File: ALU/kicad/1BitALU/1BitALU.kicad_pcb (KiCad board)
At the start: 2 copper layers, 165.1 x 120.7 mm, 55 parts, among them P1 CONN_6, P2 CONN_2, P3 Power, U1 xor3a, U10 and3a, U11 or2a, U12 and3b, U13 inv3b, U14 and3c, U15 or3a, U16 xor1b, U17 xor1a, U18 xor2b, U19 and4a, U2 and2a, U20 xor2a, U21 and4b, U22 and4c, U23 or3b, U24 and5a, U25 and5b, U26 inv5c, U27 and5c, U28 or3c, U29 and6a, U3 xor3b, U30 inv6b, U31 and6b, U32 inv6c, U33 and6c, U34 or3d, U4 and2b, U5 or1b, U6 and1a, U7 and1b, U8 or1a, U9 or2b

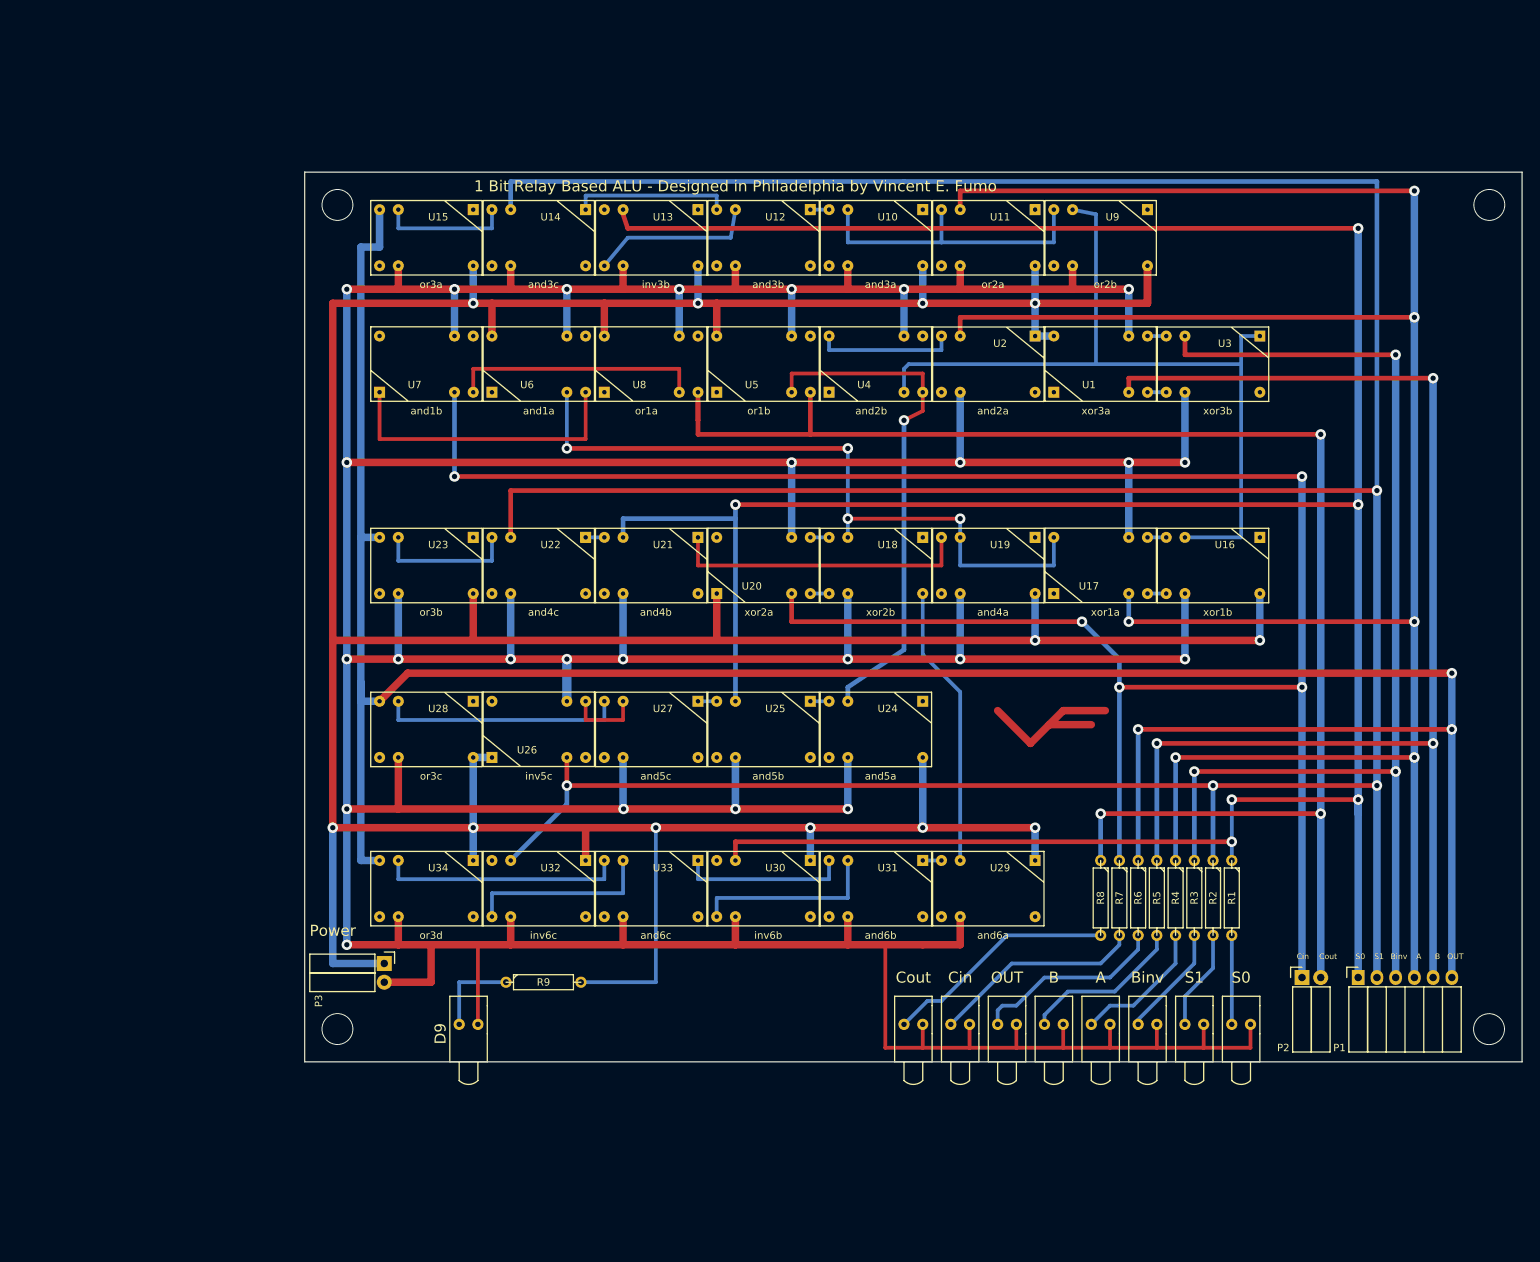
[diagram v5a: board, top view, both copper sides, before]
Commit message: puts bus connectors on side
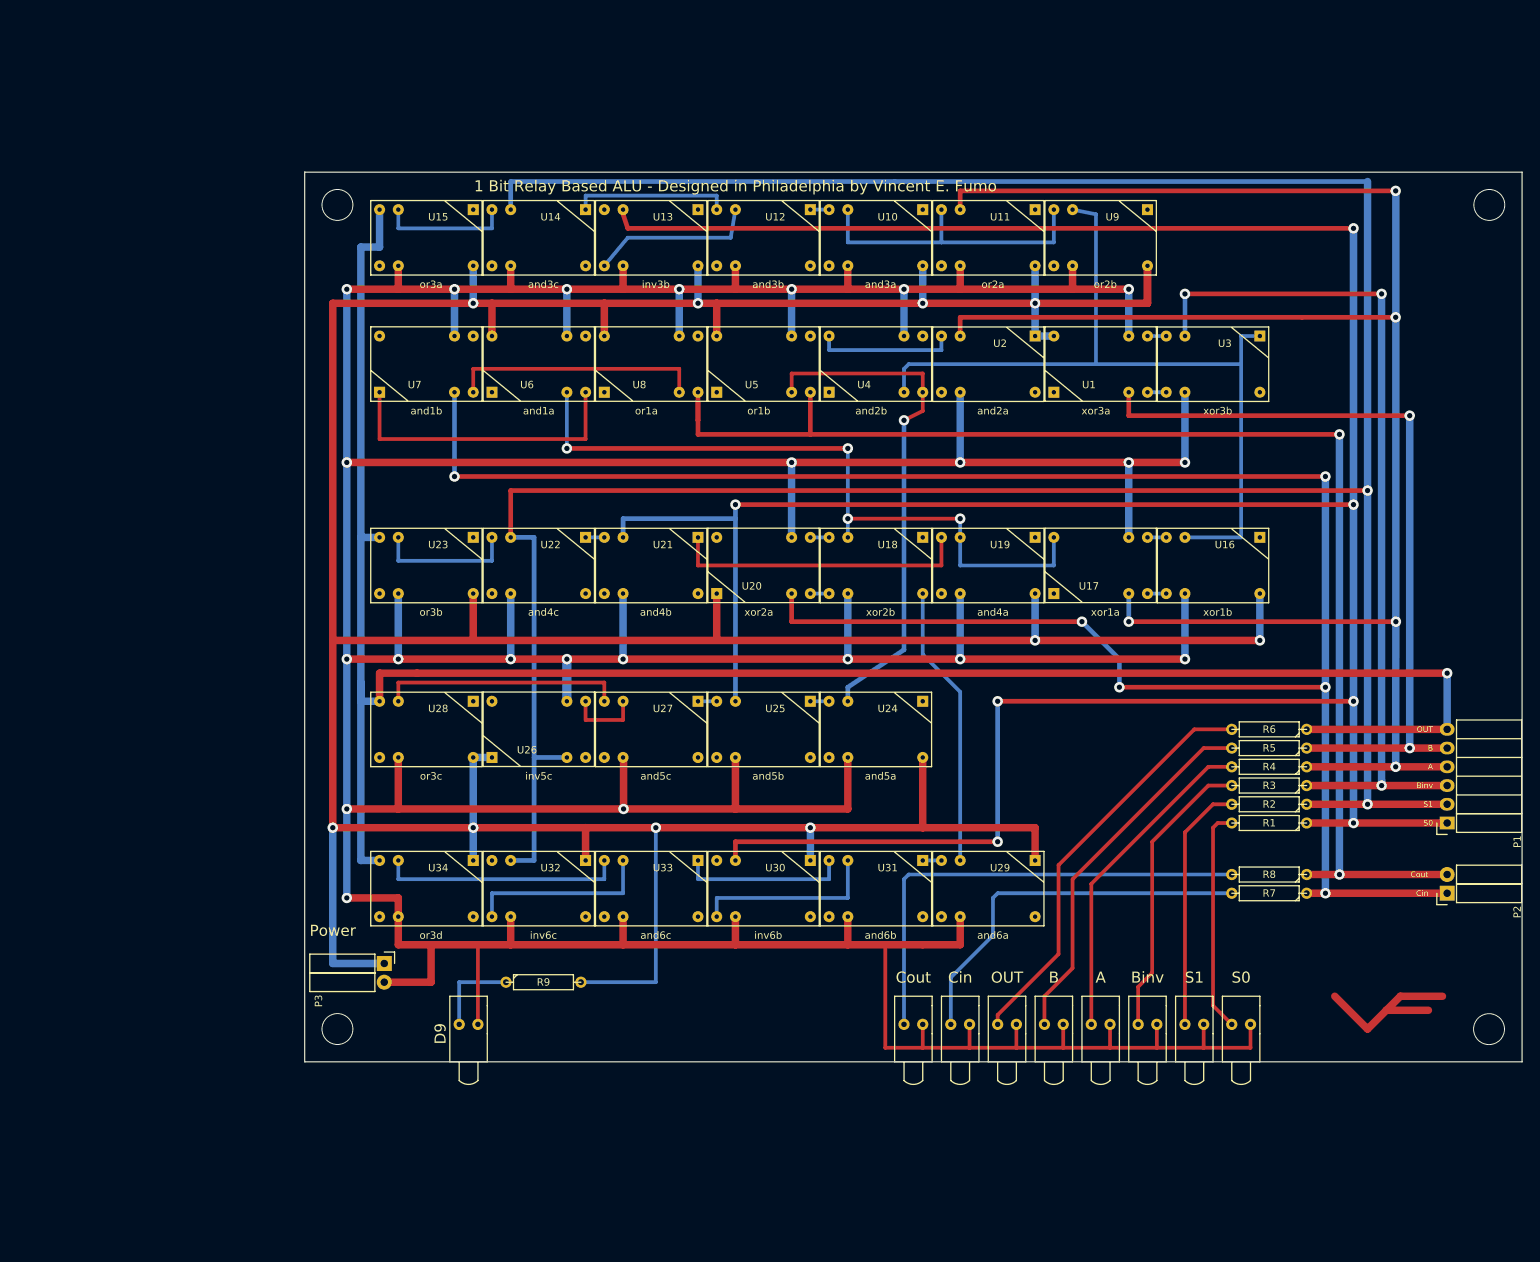
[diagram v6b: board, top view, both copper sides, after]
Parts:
- moved R6 29.0 mm to (183.2, 110.8), turned to 180 degrees
- moved R5 25.4 mm to (183.2, 113.3), turned to 180 degrees
- moved P1 24.2 mm to (207.3, 123.5), turned to 90 degrees
- moved R8 23.1 mm to (183.2, 130.5), turned to 180 degrees
- moved P2 22.8 mm to (207.3, 133.0), turned to 90 degrees
- moved R4 21.8 mm to (183.2, 115.9), turned to 180 degrees
- moved R7 20.3 mm to (183.2, 133.0), turned to 180 degrees
- moved R3 18.3 mm to (183.2, 118.4), turned to 180 degrees
- moved R2 14.8 mm to (183.2, 121.0), turned to 180 degrees
- moved R1 11.4 mm to (183.2, 123.5), turned to 180 degrees
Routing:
- net S1 Bus: track 490.2 -> 400.7 mm, vias 4 -> 2
- net OUT: track 349.6 -> 276.2 mm, vias 3 -> 1
- net B: track 177.8 -> 105.4 mm, vias 3 -> 2
- net A: track 324.5 -> 260.4 mm, vias 6 -> 5
- net Binv: track 154.9 -> 118.1 mm
- net Net-(D8-Pad1): track 31.7 -> 64.4 mm
- net Net-(D6-Pad1): track 26.3 -> 56.1 mm
- net Cout: track 208.3 -> 179.7 mm, vias 3 -> 2
- net Net-(D5-Pad1): track 22.1 -> 50.2 mm
- net Net-(D4-Pad1): track 18.7 -> 44.7 mm
- net Net-(D3-Pad1): track 15.2 -> 40.1 mm
- net Net-(D7-Pad1): track 28.6 -> 52.2 mm
- net Net-(D2-Pad1): track 13.6 -> 34.0 mm
- net Net-(D1-Pad1): track 12.1 -> 30.5 mm
- net Cin: track 296.7 -> 287.2 mm, vias 5 -> 6
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
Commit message: cleanup
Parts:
- moved P3 8.64 mm to (56.2, 137.5)
- moved R9 6.63 mm to (78.4, 143.2)
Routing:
- net +5V: track 574.7 -> 562.0 mm, vias 10 -> 9
- net Net-(D9-Pad1): track 12.1 -> 7.62 mm
- net GND: track 890.4 -> 888.5 mm
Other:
- board size 165.1 x 120.7 mm -> 171.5 x 123.2 mm
